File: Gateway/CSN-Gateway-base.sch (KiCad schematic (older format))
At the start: 67 parts, among them IC1 ATMEGA328-A, IC2 FT232RL, P1 USB_MINI, P2 CONN4, P3 CONN_ICSP, P4 CONN_OLED_SCREEN, P5 CONN6, P8 CONN_NRF24L01, Q1 2N2222, SW1 SW_PUSH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

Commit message: Split project into 2 sch + 2 pcb (screen + base)
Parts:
- removed C15, C19: 100nF, Capacitors_SMD:C_0805_HandSoldering, symbol C
- removed C2: 0.1uF, Capacitors_SMD:C_0805_HandSoldering, symbol C
- removed D1: LED_RABG, symbol LED_RABG
- removed IC2: FT232RL, Housings_SSOP:SSOP-28_5.3x10.2mm_Pitch0.65mm, symbol FT232RL
- removed P1: USB_MINI, symbol USB_OTG
- removed P4: CONN_OLED_SCREEN, symbol CONN_01X04
- removed R15, R27: 10K, Resistors_SMD:R_0805_HandSoldering, symbol R
- removed R16, R22, R23: 100, Resistors_SMD:R_0805_HandSoldering, symbol R
- removed R20: 4k7, Resistors_SMD:R_0805_HandSoldering, symbol R
- removed R21: 10k, Resistors_SMD:R_0805_HandSoldering, symbol R
- removed SW1, SW2: SW_PUSH, symbol SW_PUSH
- added P1: CONN_02X06, symbol CONN_02X06
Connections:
- net labels added: RGB1, RGB2, RGB3
- wire segments 275 -> 226
- no-connect marks 14 -> 0

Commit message: add multicomp footprint
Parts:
- P2, P5: footprint (none) -> footprints:TerminalBlock_Multicomp-5-08-6pol
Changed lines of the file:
@@
 LIBS:mysensors_sensors
 LIBS:gateway
+LIBS:CSN-Gateway-base-cache
 EELAYER 25 0
 EELAYER END
@@
 $EndComp
 $Comp
-L GND #PWR5
+L GND #PWR01
 U 1 1 582C3EF1
 P 1350 5550
-F 0 "#PWR5" H 1350 5300 50  0001 C CNN
+F 0 "#PWR01" H 1350 5300 50  0001 C CNN
 F 1 "GND" H 1350 5400 50  0000 C CNN
 F 2 "" H 1350 5550 50  0000 C CNN
@@
 $EndComp
 $Comp
-L GND #PWR12
+L GND #PWR02
 U 1 1 582C410C
 P 5000 3900
-F 0 "#PWR12" H 5000 3650 50  0001 C CNN
+F 0 "#PWR02" H 5000 3650 50  0001 C CNN
 F 1 "GND" H 5000 3750 50  0000 C CNN
 F 2 "" H 5000 3900 50  0000 C CNN
@@
 $EndComp
 $Comp
-L GND #PWR2
+L GND #PWR03
 U 1 1 582C5420
 P 800 4250
-F 0 "#PWR2" H 800 4000 50  0001 C CNN
+F 0 "#PWR03" H 800 4000 50  0001 C CNN
 F 1 "GND" H 800 4100 50  0000 C CNN
 F 2 "" H 800 4250 50  0000 C CNN
@@
 $EndComp
 $Comp
-L VCC #PWR4
+L VCC #PWR04
 U 1 1 582C5592
 P 1150 2850
-F 0 "#PWR4" H 1150 2700 50  0001 C CNN
+F 0 "#PWR04" H 1150 2700 50  0001 C CNN
 F 1 "VCC" H 1150 3000 50  0000 C CNN
 F 2 "" H 1150 2850 50  0000 C CNN
@@
 $EndComp
 $Comp
-L VCC #PWR9
+L VCC #PWR05
 U 1 1 582C58DF
 P 4450 4350
-F 0 "#PWR9" H 4450 4200 50  0001 C CNN
+F 0 "#PWR05" H 4450 4200 50  0001 C CNN
 F 1 "VCC" H 4450 4500 50  0000 C CNN
 F 2 "" H 4450 4350 50  0000 C CNN
@@
 TXO
 $Comp
-L PWR_FLAG #FLG2
+L PWR_FLAG #FLG06
 U 1 1 582C6C8A
 P 3750 1300
-F 0 "#FLG2" H 3750 1395 50  0001 C CNN
+F 0 "#FLG06" H 3750 1395 50  0001 C CNN
 F 1 "PWR_FLAG" H 3750 1480 50  0000 C CNN
 F 2 "" H 3750 1300 50  0000 C CNN
@@
 $EndComp
 $Comp
-L VCC #PWR7
+L VCC #PWR07
 U 1 1 582C6CAE
 P 3400 1100
-F 0 "#PWR7" H 3400 950 50  0001 C CNN
+F 0 "#PWR07" H 3400 950 50  0001 C CNN
 F 1 "VCC" H 3400 1250 50  0000 C CNN
 F 2 "" H 3400 1100 50  0000 C CNN
@@
 $EndComp
 $Comp
-L PWR_FLAG #FLG1
+L PWR_FLAG #FLG08
 U 1 1 582C6CD2
 P 2100 2500
-F 0 "#FLG1" H 2100 2595 50  0001 C CNN
+F 0 "#FLG08" H 2100 2595 50  0001 C CNN
 F 1 "PWR_FLAG" H 2100 2680 50  0000 C CNN
 F 2 "" H 2100 2500 50  0000 C CNN
@@
 $EndComp
 $Comp
-L GND #PWR8
+L GND #PWR09
 U 1 1 582C7255
 P 3400 2450
-F 0 "#PWR8" H 3400 2200 50  0001 C CNN
+F 0 "#PWR09" H 3400 2200 50  0001 C CNN
 F 1 "GND" H 3400 2300 50  0000 C CNN
 F 2 "" H 3400 2450 50  0000 C CNN
@@
 MOSI
 $Comp
-L GND #PWR17
+L GND #PWR010
 U 1 1 582C8778
 P 8800 1050
-F 0 "#PWR17" H 8800 800 50  0001 C CNN
+F 0 "#PWR010" H 8800 800 50  0001 C CNN
 F 1 "GND" H 8800 900 50  0000 C CNN
 F 2 "" H 8800 1050 50  0000 C CNN
@@
 $EndComp
 $Comp
-L VCC #PWR16
+L VCC #PWR011
 U 1 1 582C87A0
 P 8800 750
-F 0 "#PWR16" H 8800 600 50  0001 C CNN
+F 0 "#PWR011" H 8800 600 50  0001 C CNN
 F 1 "VCC" H 8800 900 50  0000 C CNN
 F 2 "" H 8800 750 50  0000 C CNN
@@
 $EndComp
 $Comp
-L VCC #PWR22
+L VCC #PWR012
 U 1 1 58385B4B
 P 9650 2650
-F 0 "#PWR22" H 9650 2500 50  0001 C CNN
+F 0 "#PWR012" H 9650 2500 50  0001 C CNN
 F 1 "VCC" H 9650 2800 50  0000 C CNN
 F 2 "" H 9650 2650 50  0000 C CNN
@@
 $EndComp
 $Comp
-L GND #PWR23
+L GND #PWR013
 U 1 1 58385B7D
 P 9650 3850
-F 0 "#PWR23" H 9650 3600 50  0001 C CNN
+F 0 "#PWR013" H 9650 3600 50  0001 C CNN
 F 1 "GND" H 9650 3700 50  0000 C CNN
 F 2 "" H 9650 3850 50  0000 C CNN
@@
 $EndComp
 $Comp
-L VCC #PWR27
+L VCC #PWR014
 U 1 1 58387833
 P 11000 2650
-F 0 "#PWR27" H 11000 2500 50  0001 C CNN
+F 0 "#PWR014" H 11000 2500 50  0001 C CNN
 F 1 "VCC" H 11000 2800 50  0000 C CNN
 F 2 "" H 11000 2650 50  0000 C CNN
@@
 $EndComp
 $Comp
-L GND #PWR28
+L GND #PWR015
 U 1 1 58387839
 P 11000 3850
-F 0 "#PWR28" H 11000 3600 50  0001 C CNN
+F 0 "#PWR015" H 11000 3600 50  0001 C CNN
 F 1 "GND" H 11000 3700 50  0000 C CNN
 F 2 "" H 11000 3850 50  0000 C CNN
@@
 $EndComp
 $Comp
-L VCC #PWR25
+L VCC #PWR016
 U 1 1 58387BF8
 P 11000 850
-F 0 "#PWR25" H 11000 700 50  0001 C CNN
+F 0 "#PWR016" H 11000 700 50  0001 C CNN
 F 1 "VCC" H 11000 1000 50  0000 C CNN
 F 2 "" H 11000 850 50  0000 C CNN
@@
 $EndComp
 $Comp
-L GND #PWR26
+L GND #PWR017
 U 1 1 58387BFE
 P 11000 2050
-F 0 "#PWR26" H 11000 1800 50  0001 C CNN
+F 0 "#PWR017" H 11000 1800 50  0001 C CNN
 F 1 "GND" H 11000 1900 50  0000 C CNN
 F 2 "" H 11000 2050 50  0000 C CNN
@@
 $EndComp
 $Comp
-L GND #PWR21
+L GND #PWR018
 U 1 1 5838AB1A
 P 9450 6200
-F 0 "#PWR21" H 9450 5950 50  0001 C CNN
+F 0 "#PWR018" H 9450 5950 50  0001 C CNN
 F 1 "GND" H 9450 6050 50  0000 C CNN
 F 2 "" H 9450 6200 50  0000 C CNN
@@
 $EndComp
 $Comp
-L VCC #PWR20
+L VCC #PWR019
 U 1 1 5838AD80
 P 9450 4400
-F 0 "#PWR20" H 9450 4250 50  0001 C CNN
+F 0 "#PWR019" H 9450 4250 50  0001 C CNN
 F 1 "VCC" H 9450 4550 50  0000 C CNN
 F 2 "" H 9450 4400 50  0000 C CNN
@@
 $EndComp
 $Comp
-L VCC #PWR1
+L VCC #PWR020
 U 1 1 58394BCB
 P 700 6400
-F 0 "#PWR1" H 700 6250 50  0001 C CNN
+F 0 "#PWR020" H 700 6250 50  0001 C CNN
 F 1 "VCC" H 700 6550 50  0000 C CNN
 F 2 "" H 700 6400 50  0000 C CNN
@@
 $EndComp
 $Comp
-L GND #PWR10
+L GND #PWR021
 U 1 1 58394C21
 P 4500 7400
-F 0 "#PWR10" H 4500 7150 50  0001 C CNN
+F 0 "#PWR021" H 4500 7150 50  0001 C CNN
 F 1 "GND" H 4500 7250 50  0000 C CNN
 F 2 "" H 4500 7400 50  0000 C CNN
@@
 RS485_EN
 $Comp
-L GND #PWR6
+L GND #PWR022
 U 1 1 583A146D
 P 1750 7500
-F 0 "#PWR6" H 1750 7250 50  0001 C CNN
+F 0 "#PWR022" H 1750 7250 50  0001 C CNN
 F 1 "GND" H 1750 7350 50  0000 C CNN
 F 2 "" H 1750 7500 50  0000 C CNN
@@
 $EndComp
 $Comp
-L GND #PWR24
+L GND #PWR023
 U 1 1 583B1A4D
 P 9900 4900
-F 0 "#PWR24" H 9900 4650 50  0001 C CNN
+F 0 "#PWR023" H 9900 4650 50  0001 C CNN
 F 1 "GND" H 9900 4750 50  0000 C CNN
 F 2 "" H 9900 4900 50  0000 C CNN
@@
 BTN1
 $Comp
-L GND #PWR3
+L GND #PWR024
 U 1 1 583CE9C7
 P 1000 3400
-F 0 "#PWR3" H 1000 3150 50  0001 C CNN
+F 0 "#PWR024" H 1000 3150 50  0001 C CNN
 F 1 "GND" H 1000 3250 50  0000 C CNN
 F 2 "" H 1000 3400 50  0000 C CNN
@@
 SDA
 $Comp
-L GND #PWR15
+L GND #PWR025
 U 1 1 583D4DFC
 P 5900 7200
-F 0 "#PWR15" H 5900 6950 50  0001 C CNN
+F 0 "#PWR025" H 5900 6950 50  0001 C CNN
 F 1 "GND" H 5900 7050 50  0000 C CNN
 F 2 "" H 5900 7200 50  0000 C CNN
@@
 $EndComp
 $Comp
-L VCC #PWR14
+L VCC #PWR026
 U 1 1 583D5A04
 P 5900 6400
-F 0 "#PWR14" H 5900 6250 50  0001 C CNN
+F 0 "#PWR026" H 5900 6250 50  0001 C CNN
 F 1 "VCC" H 5900 6550 50  0000 C CNN
 F 2 "" H 5900 6400 50  0000 C CNN
@@
 F 0 "P2" H 1150 2250 50  0000 C CNN
 F 1 "CONN4" H 1150 1250 50  0000 C CNN
-F 2 "" H 1150 450 50  0001 C CNN
+F 2 "footprints:TerminalBlock_Multicomp-5-08-6pol" H 1150 450 50  0001 C CNN
 F 3 "" H 1150 450 50  0000 C CNN
 	1    1150 1650
@@
 F 0 "P5" H 9450 2070 50  0000 C CNN
 F 1 "CONN6" H 9450 1050 50  0000 C CNN
-F 2 "" H 9450 300 50  0001 C CNN
+F 2 "footprints:TerminalBlock_Multicomp-5-08-6pol" H 9450 300 50  0001 C CNN
 F 3 "" H 9450 300 50  0000 C CNN
 	1    9450 1500
@@
 $EndComp
 $Comp
-L VCC #PWR18
+L VCC #PWR027
 U 1 1 58407738
 P 8800 2650
-F 0 "#PWR18" H 8800 2500 50  0001 C CNN
+F 0 "#PWR027" H 8800 2500 50  0001 C CNN
 F 1 "VCC" H 8800 2800 50  0000 C CNN
 F 2 "" H 8800 2650 50  0000 C CNN
@@
 $EndComp
 $Comp
-L GND #PWR19
+L GND #PWR028
 U 1 1 5840773E
 P 8800 3850
-F 0 "#PWR19" H 8800 3600 50  0001 C CNN
+F 0 "#PWR028" H 8800 3600 50  0001 C CNN
 F 1 "GND" H 8800 3700 50  0000 C CNN
 F 2 "" H 8800 3850 50  0000 C CNN
@@
 RST
 $Comp
-L VCC #PWR13
+L VCC #PWR029
 U 1 1 58409376
 P 5400 1250
-F 0 "#PWR13" H 5400 1100 50  0001 C CNN
+F 0 "#PWR029" H 5400 1100 50  0001 C CNN
 F 1 "VCC" H 5400 1400 50  0000 C CNN
 F 2 "" H 5400 1250 50  0000 C CNN
@@
 $EndComp
 $Comp
-L GND #PWR11
+L GND #PWR030
 U 1 1 58409426
 P 4950 1450
-F 0 "#PWR11" H 4950 1200 50  0001 C CNN
+F 0 "#PWR030" H 4950 1200 50  0001 C CNN
 F 1 "GND" H 4950 1300 50  0000 C CNN
 F 2 "" H 4950 1450 50  0000 C CNN

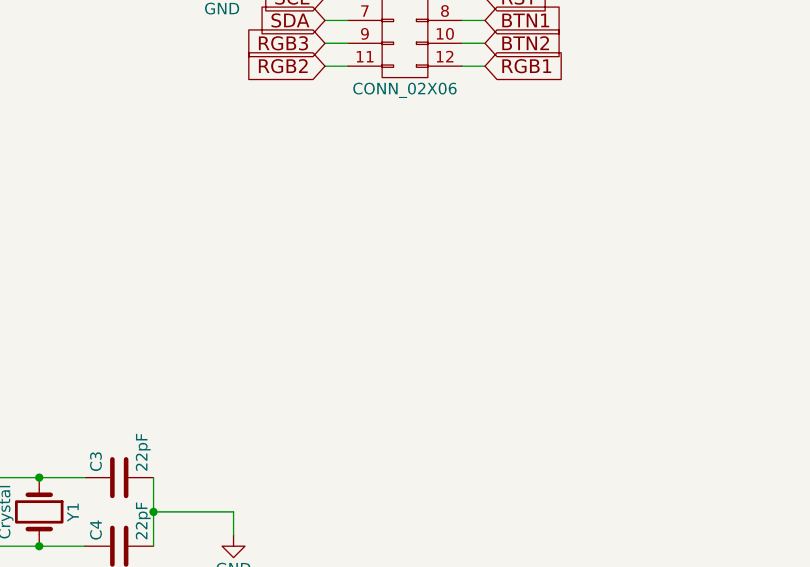
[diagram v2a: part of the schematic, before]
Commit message: add all missing footprints
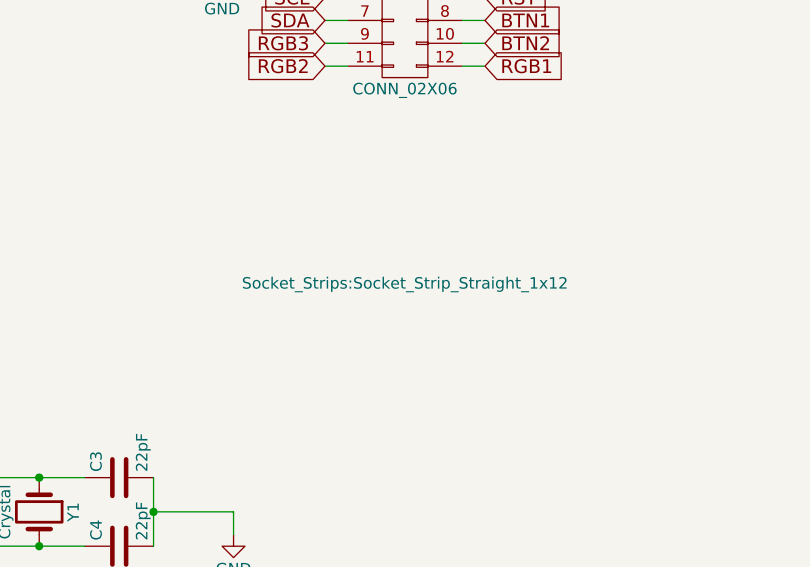
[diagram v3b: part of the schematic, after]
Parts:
- P1: footprint (none) -> Socket_Strips:Socket_Strip_Straight_1x12
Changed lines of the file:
@@
 F 0 "P1" H 5750 1950 50  0000 C CNN
 F 1 "CONN_02X06" H 5750 1250 50  0000 C CNN
-F 2 "" H 5750 400 50  0000 C CNN
+F 2 "Socket_Strips:Socket_Strip_Straight_1x12" H 5750 400 50  0000 C CNN
 F 3 "" H 5750 400 50  0000 C CNN
 	1    5750 1600

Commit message: begin placement of compo on base pcb
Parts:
- C10, C13, C9: footprint Capacitors_SMD:C_0805_HandSoldering -> SMD_Packages:SMD-1206_Pol
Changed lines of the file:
@@
 F 0 "C9" H 2325 7100 50  0000 L CNN
 F 1 "10uF" H 2325 6900 50  0000 L CNN
-F 2 "Capacitors_SMD:C_0805_HandSoldering" H 2338 6850 50  0001 C CNN
+F 2 "SMD_Packages:SMD-1206_Pol" H 2338 6850 50  0001 C CNN
 F 3 "" H 2300 7000 50  0000 C CNN
 	1    2300 7000
@@
 F 0 "C10" H 775 7100 50  0000 L CNN
 F 1 "10uF" H 775 6900 50  0000 L CNN
-F 2 "Capacitors_SMD:C_0805_HandSoldering" H 788 6850 50  0001 C CNN
+F 2 "SMD_Packages:SMD-1206_Pol" H 788 6850 50  0001 C CNN
 F 3 "" H 750 7000 50  0000 C CNN
 	1    750  7000
@@
 F 0 "C13" H 9675 5150 50  0000 L CNN
 F 1 "10uF" H 9675 4950 50  0000 L CNN
-F 2 "Capacitors_SMD:C_0805_HandSoldering" H 9688 4900 50  0001 C CNN
+F 2 "SMD_Packages:SMD-1206_Pol" H 9688 4900 50  0001 C CNN
 F 3 "" H 9650 5050 50  0000 C CNN
 	1    9650 5050

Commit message: Finish base pcb routing and adjust all mounting holes
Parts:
- renumbered P8 to RADIO1
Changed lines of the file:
@@
 LIBS:mysensors_memories
 LIBS:mysensors_network
-LIBS:mysensors_radios
 LIBS:mysensors_regulators
 LIBS:mysensors_security
 LIBS:mysensors_sensors
+LIBS:mysensors_radios
 LIBS:gateway
 LIBS:CSN-Gateway-base-cache
@@
 SCL
 Text GLabel 3450 4000 2    60   Input ~ 0
-A0
+A2
 Text GLabel 3450 4100 2    60   Input ~ 0
-A1
+A3
 Text GLabel 3450 4200 2    60   Input ~ 0
-BTN2
+RS485_TX
 $Comp
 L R R3
@@
 RS485_RX
 Text GLabel 3450 5150 2    60   Input ~ 0
-RS485_TX
+BTN1
 Text GLabel 3450 5050 2    60   Input ~ 0
 RS485_RX
 $Comp
-L CONN_02X04 P8
+L CONN_02X04 RADIO1
 U 1 1 58394785
 P 4000 7000
-F 0 "P8" H 4000 7250 50  0000 C CNN
+F 0 "RADIO1" H 4000 7250 50  0000 C CNN
 F 1 "CONN_NRF24L01" H 4000 6750 50  0000 C CNN
 F 2 "mysensors_radios:NRF24L01" H 4000 5800 50  0001 C CNN
@@
 IRQ
 Text GLabel 3450 5250 2    60   Input ~ 0
-RS485_EN
+RGB3
 $Comp
 L GND #PWR022
@@
 $EndComp
 Text GLabel 3450 3150 2    60   Input ~ 0
-BTN1
+RGB1
 $Comp
 L GND #PWR024
@@
 $EndComp
 Text GLabel 1350 4500 0    60   Input ~ 0
-A2
+A0
 $Comp
 L CP1 C17
@@
 	7950 2800 8300 2800
 Text GLabel 1350 4600 0    60   Input ~ 0
-A3
+A1
 Wire Wire Line
 	1350 4600 1450 4600
@@
 F 0 "P1" H 5750 1950 50  0000 C CNN
 F 1 "CONN_02X06" H 5750 1250 50  0000 C CNN
-F 2 "Socket_Strips:Socket_Strip_Straight_1x12" H 5750 400 50  0000 C CNN
+F 2 "Socket_Strips:Socket_Strip_Straight_1x12" H 5750 1150 50  0000 C CNN
 F 3 "" H 5750 400 50  0000 C CNN
 	1    5750 1600
@@
 	5400 1850 5500 1850
 Text GLabel 3450 4300 2    60   Input ~ 0
-RGB1
+RS485_EN
 Text GLabel 3450 5350 2    60   Input ~ 0
+BTN2
+Text GLabel 3450 5450 2    60   Input ~ 0
 RGB2
-Text GLabel 3450 5450 2    60   Input ~ 0
-RGB3
 Wire Wire Line
 	3350 5350 3450 5350

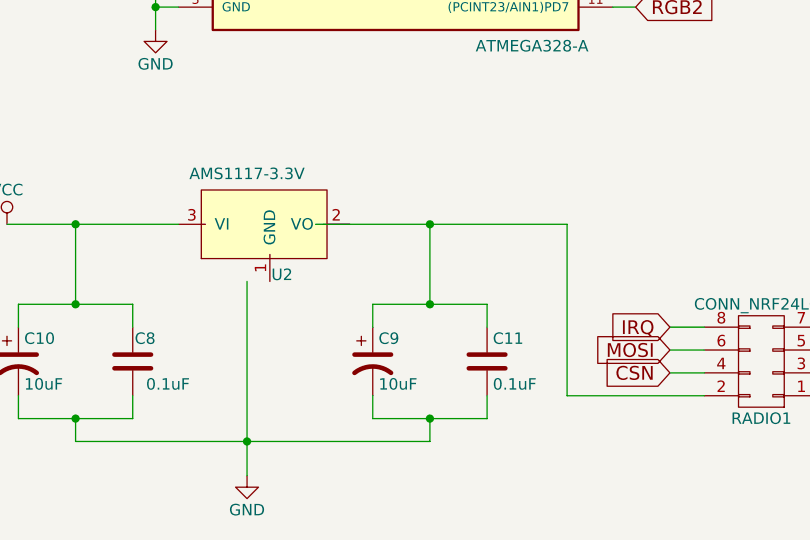
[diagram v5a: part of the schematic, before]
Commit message: pin 4 of ams1117 to gnd
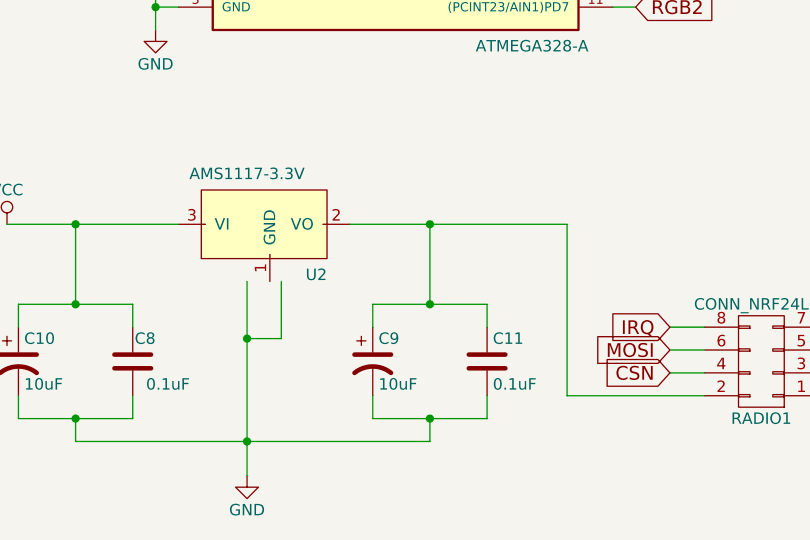
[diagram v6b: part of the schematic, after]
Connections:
- wire segments 226 -> 228
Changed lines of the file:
@@
 U 1 1 583D40E0
 P 1850 6400
-F 0 "U2" H 1950 6150 50  0000 R BNN
+F 0 "U2" H 2100 6150 50  0000 R BNN
 F 1 "AMS1117-3.3V" H 1750 6650 50  0000 C TNN
 F 2 "TO_SOT_Packages_SMD:SOT-223" H 1750 6450 60  0001 C CNN
@@
 Wire Wire Line
 	3900 4350 4000 4350
-Wire Wire Line
-	2050 6400 3150 6400
 Wire Wire Line
 	700  6400 1450 6400
@@
 Wire Wire Line
 	3350 4300 3450 4300
+Wire Wire Line
+	1900 6650 1900 6900
+Wire Wire Line
+	1900 6900 1750 6900
+Connection ~ 1750 6900
+Wire Wire Line
+	2200 6400 3150 6400
 $EndSCHEMATC

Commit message: fix wrong footprints
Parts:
- Q1: symbol Q_NPN_BCE -> Q_NPN_BCEG
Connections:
- wire segments 228 -> 226
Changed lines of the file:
@@
 $EndComp
 $Comp
-L Q_NPN_BCE Q1
+L Q_NPN_BCEG Q1
 U 1 1 583D2BBC
 P 2750 1400
@@
 	700  6400 1450 6400
 Wire Wire Line
-	1750 6650 1750 7500
-Wire Wire Line
 	2550 6400 2550 6750
 Wire Wire Line
@@
 Wire Wire Line
 	1000 7350 2550 7350
-Connection ~ 1750 7350
 Connection ~ 1000 7250
 Wire Wire Line
@@
 	3350 4300 3450 4300
 Wire Wire Line
-	1900 6650 1900 6900
-Wire Wire Line
-	1900 6900 1750 6900
-Connection ~ 1750 6900
-Wire Wire Line
 	2200 6400 3150 6400
+Wire Wire Line
+	1850 6650 1850 7350
+Connection ~ 1850 7350
 $EndSCHEMATC

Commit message: Fix footprints for power supply components
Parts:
- D2: symbol TL431 -> TL431-RESCUE-CSN-Gateway-base
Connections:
- net GND: now also C10.2, C11.2, C8.1, C9.2, U2.1 (GND)
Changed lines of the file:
@@
 EESchema Schematic File Version 2
+LIBS:CSN-Gateway-base-rescue
 LIBS:power
 LIBS:device
@@
 L GND #PWR022
 U 1 1 583A146D
-P 1750 7500
-F 0 "#PWR022" H 1750 7250 50  0001 C CNN
-F 1 "GND" H 1750 7350 50  0000 C CNN
-F 2 "" H 1750 7500 50  0000 C CNN
-F 3 "" H 1750 7500 50  0000 C CNN
-	1    1750 7500
+P 1850 7500
+F 0 "#PWR022" H 1850 7250 50  0001 C CNN
+F 1 "GND" H 1850 7350 50  0000 C CNN
+F 2 "" H 1850 7500 50  0000 C CNN
+F 3 "" H 1850 7500 50  0000 C CNN
+	1    1850 7500
 	1    0    0    -1
 $EndComp
@@
 $EndComp
 $Comp
-L TL431 D2
+L TL431-RESCUE-CSN-Gateway-base D2
 U 1 1 583D26E5
 P 2750 1950
@@
 	2200 6400 3150 6400
 Wire Wire Line
-	1850 6650 1850 7350
+	1850 6650 1850 7500
 Connection ~ 1850 7350
 $EndSCHEMATC
